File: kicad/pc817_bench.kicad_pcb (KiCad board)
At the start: 2 copper layers, 66 x 53.3 mm, 27 parts, among them J1 24V, e-stops, lidars, U1 PC817, U2 PC817, U3 PC817, U4 PC817

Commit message: Proto-shield: terminals as soldered (three 3-way 2.54 mm blocks at columns 8-10, 13-15, 18-20)
Supply on J1, e-stops on J2, lidars on J3. Fuse moved to row 5 (columns 8 and 6),
with a wire from the fused side to the ES+ screw. Schematic, plan and KiCad model
updated together; model matches the schematic.

Co-Authored-By: Claude Fable 5.1 <noreply@anthropic.com>
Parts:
- added J2: e-stops, TerminalBlock:TerminalBlock_Xinya_XY308-2.54-3P_1x03_P2.54mm_Horizontal, F.Cu at (94.6, 97.8)
- added J3: lidars, TerminalBlock:TerminalBlock_Xinya_XY308-2.54-3P_1x03_P2.54mm_Horizontal, F.Cu at (94.6, 85.1)
- J1: value 24V, e-stops, lidars -> 24 V supply; footprint TerminalBlock_Phoenix:TerminalBlock_Phoenix_MKDS-1,5-8-5.08_1x08_P5.08mm_Horizontal -> TerminalBlock:TerminalBlock_Xinya_XY308-2.54-3P_1x03_P2.54mm_Horizontal
- moved F1 5.68 mm to (104.8, 110.5), turned to -90 degrees
- moved J1 5.08 mm to (94.6, 110.5)
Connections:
- J1 pad 2: /+24V -> /GND_24V
- J1 pad 3: /ES1 -> /GND_24V
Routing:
- net /GND_24V: track 147.3 -> 157.5 mm
- net Net-(J1-24V_IN): track 12.7 -> 10.2 mm

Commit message: Proto-shield: fuse as built (flat in row 4, legs at columns 8 and 13)
It joins the 24V screw to the ES+ screw directly, so the extra wire is gone.

Co-Authored-By: Claude Fable 5.1 <noreply@anthropic.com>
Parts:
- F1: footprint Fuse:Fuse_Littelfuse_372_D8.50mm -> Resistor_THT:R_Axial_DIN0309_L9.0mm_D3.2mm_P12.70mm_Horizontal
- moved F1 2.54 mm to (102.2, 110.5), turned to 90 degrees
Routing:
- net /+24V: track 12.7 -> 7.62 mm
- net Net-(J1-24V_IN): track 10.2 -> 7.62 mm

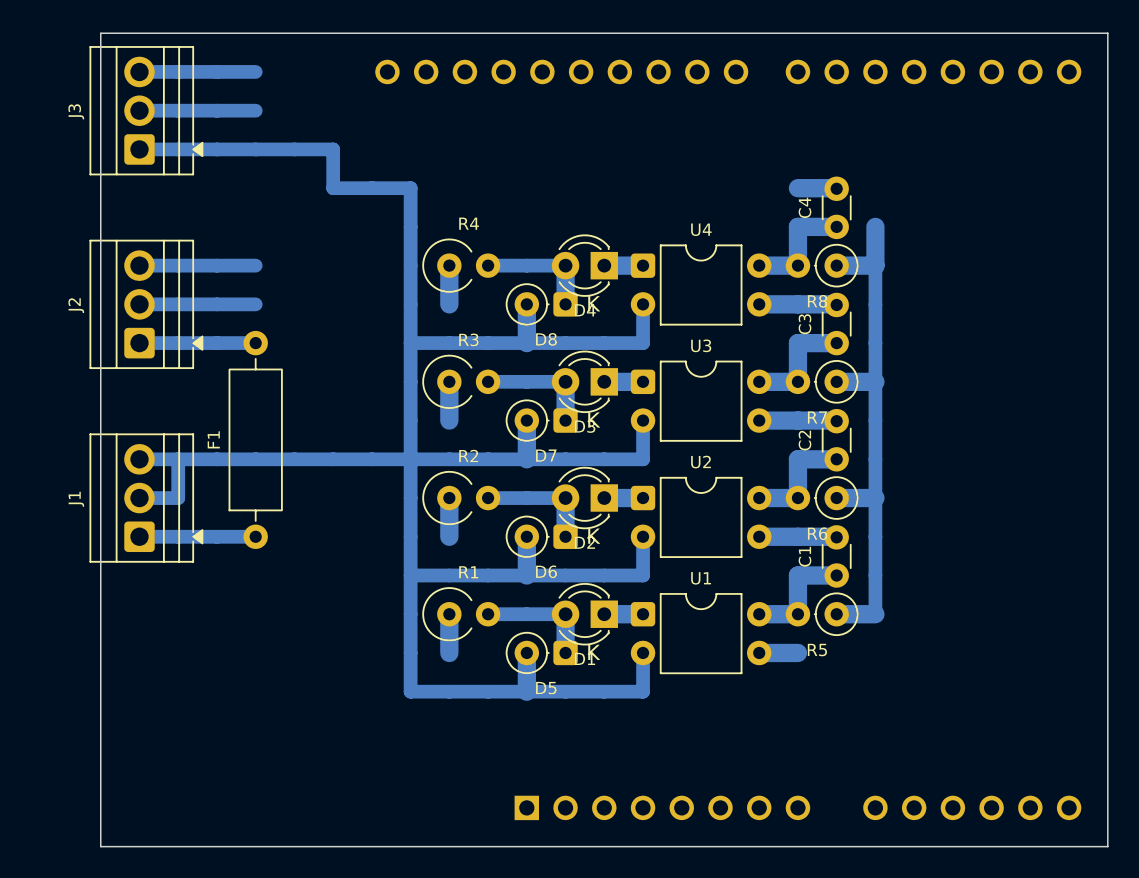
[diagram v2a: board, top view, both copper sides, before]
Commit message: Proto-shield: plan re-laid around the board as soldered
Sockets in rows 12 and 15 at columns (7,8) (10,11) (13,14) (16,17); 0V bus in
row 6 with a wire down each socket's pin-2 column. The remaining parts move to
match: each channel in one column, diode anode straight onto the 0V wire,
capacitor across the socket's logic pins. 13 insulated wires. Model matches the
schematic.

Co-Authored-By: Claude Fable 5.1 <noreply@anthropic.com>
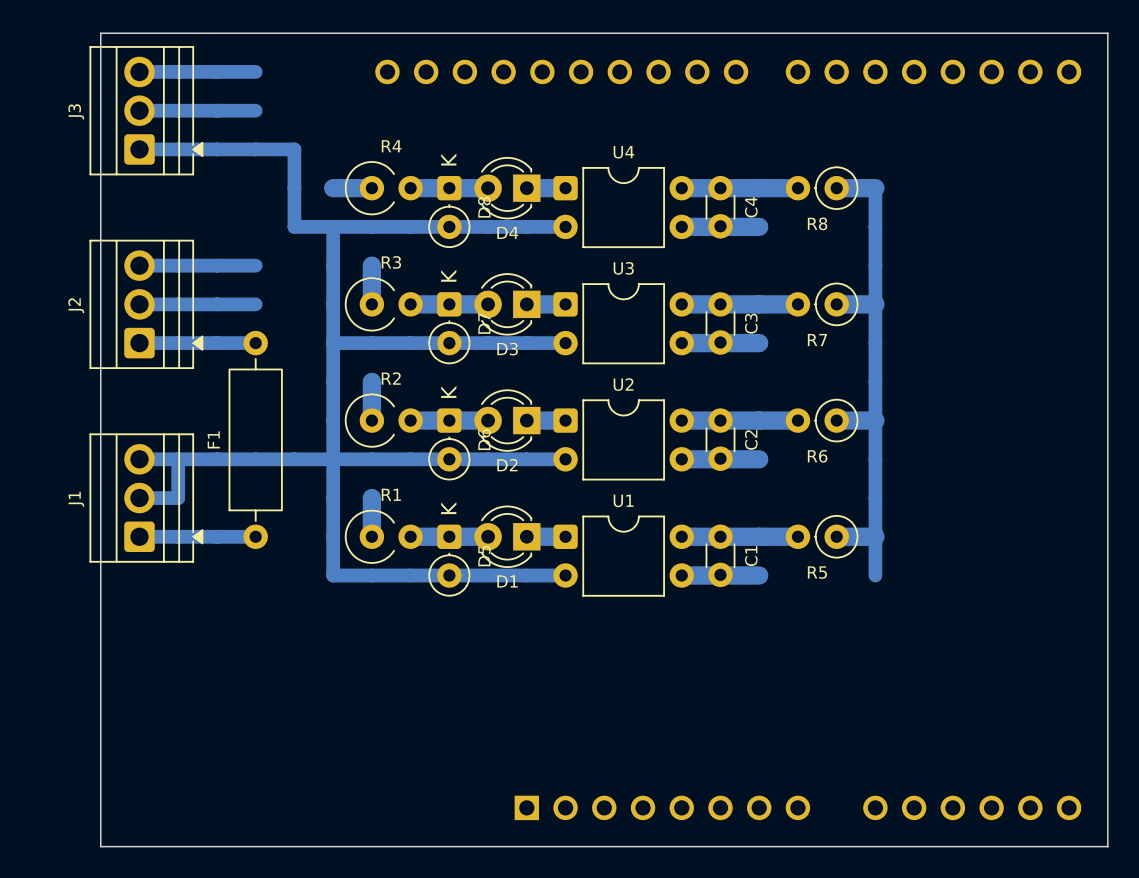
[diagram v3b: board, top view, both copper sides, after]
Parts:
- moved D6 10.8 mm to (114.9, 102.9), turned to -90 degrees
- moved D7 10.8 mm to (114.9, 95.2), turned to -90 degrees
- moved D5 10.8 mm to (114.9, 110.5), turned to -90 degrees
- moved D8 10.8 mm to (114.9, 87.6), turned to -90 degrees
- moved C2 8.03 mm to (132.7, 102.9), turned to -90 degrees
- moved C3 8.03 mm to (132.7, 95.2), turned to -90 degrees
- moved C1 8.03 mm to (132.7, 110.5), turned to -90 degrees
- moved C4 8.03 mm to (132.7, 87.6), turned to -90 degrees
- moved D1 7.18 mm to (120.0, 110.5)
- moved D2 7.18 mm to (120.0, 102.9)
- moved D3 7.18 mm to (120.0, 95.2)
- moved D4 7.18 mm to (120.0, 87.6)
- moved R1 7.18 mm to (109.8, 110.5)
- moved R2 7.18 mm to (109.8, 102.9)
- moved R3 7.18 mm to (109.8, 95.2)
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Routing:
- net /GND_24V: track 157.5 -> 119.4 mm
- net Net-(D3-A): track 7.62 -> 5.08 mm
- net Net-(D2-A): track 7.62 -> 5.08 mm
- net Net-(D4-A): track 7.62 -> 5.08 mm
- net Net-(D1-A): track 7.62 -> 5.08 mm
